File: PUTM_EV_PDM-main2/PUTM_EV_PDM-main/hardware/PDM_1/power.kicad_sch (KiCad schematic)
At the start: 20 parts, among them U2 LD1117S33TR_SOT223, U3 LM2675M-5.0/NOPB

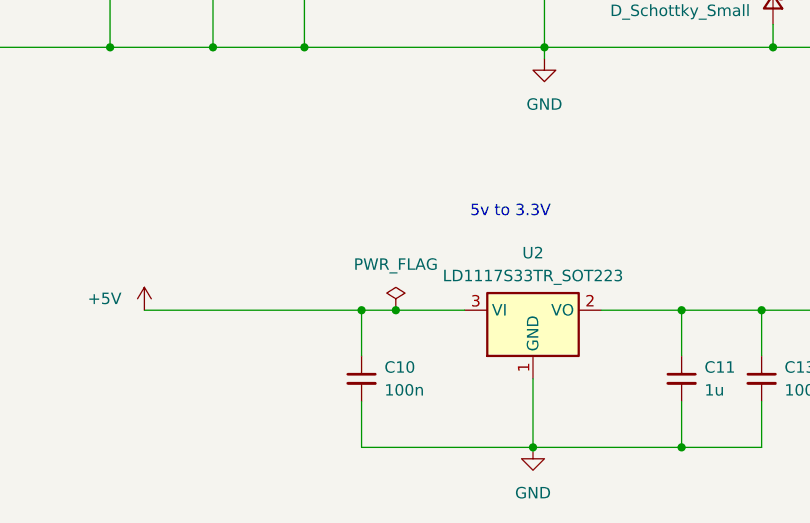
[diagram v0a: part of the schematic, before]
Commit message: Koniec połączeń sygnałów
Wszystkie sygnały z stm poprowadzone
Zmienione ułożenie połączeń do złącz
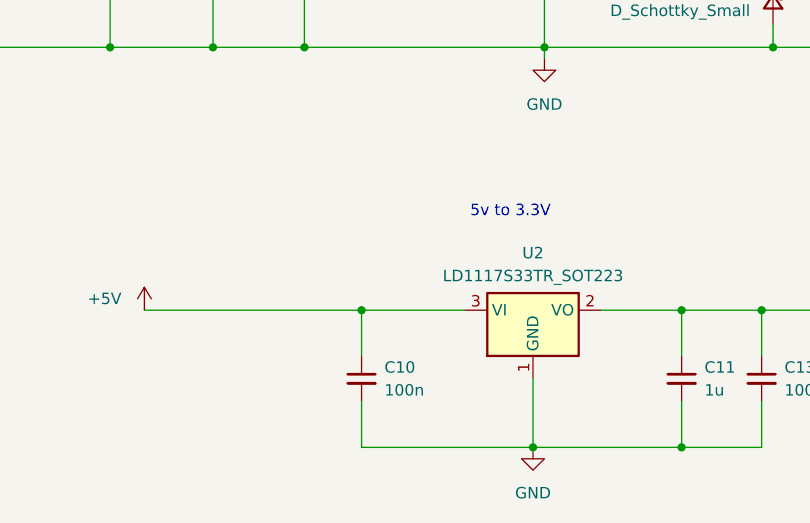
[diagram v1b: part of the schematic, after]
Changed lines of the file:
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@@
   (junction (at 228.6 87.63) (diameter 0) (color 0 0 0 0)
   )
-  (junction (at 139.7 128.27) (diameter 0) (color 0 0 0 0)
-  )
   (junction (at 95.25 77.47) (diameter 0) (color 0 0 0 0)
   )
@@
     (stroke (width 0) (type default))
   )
-  (wire (pts (xy 135.89 128.27) (xy 139.7 128.27))
-    (stroke (width 0) (type default))
-  )
   (wire (pts (xy 111.76 128.27) (xy 135.89 128.27))
     (stroke (width 0) (type default))
@@
     (stroke (width 0) (type default))
   )
-  (wire (pts (xy 139.7 128.27) (xy 147.32 128.27))
+  (wire (pts (xy 135.89 128.27) (xy 147.32 128.27))
     (stroke (width 0) (type default))
   )
@@
         )
       )
-    )
-  )
-  (symbol (lib_id "power:PWR_FLAG") (at 139.7 128.27 0) (unit 1)
-    (in_bom yes) (on_board yes) (dnp no) (fields_autoplaced)
-    (property "Reference" "#FLG02" (at 139.7 126.365 0)
-      (effects (font (size 1.27 1.27)) hide)
-    )
-    (property "Value" "PWR_FLAG" (at 139.7 123.19 0)
-      (effects (font (size 1.27 1.27)))
-    )
-    (property "Footprint" "" (at 139.7 128.27 0)
-      (effects (font (size 1.27 1.27)) hide)
-    )
-    (property "Datasheet" "~" (at 139.7 128.27 0)
-      (effects (font (size 1.27 1.27)) hide)
-    )
-    (pin "1")
-    (instances
-      (project "PDM_1"
-        (path "/b652b05a-4e3d-4ad1-b032-18886abe7d45/1367ec17-5fee-46da-adec-17b799499894"
-          (reference "#FLG02") (unit 1)
-        )
-      )
-      (project "PDM"
-        (path "/d7434f1a-7415-4eaa-a71b-b9580d7b34f2/bce9111c-7679-44f6-9761-394d41af211c"
-          (reference "#FLG02") (unit 1)
-        )
-      )
